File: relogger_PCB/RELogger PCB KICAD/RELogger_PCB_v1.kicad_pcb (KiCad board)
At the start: 2 copper layers, 115.6 x 99.1 mm, 76 parts, among them J1 RTC_MODULE, J2 Arduino_Nano_Header, J3 MICRO_SD, K1 ANEMOM1, P1 EXTERNAL PSU, P10 VANE, P11 SERIAL, P12 SOFT_SERIAL, P13 D6_D7, P14 AC_IN, P15 ANEMOM2, P2 BATTERY, P22 A_IN_45, P23 AGND_GND, P26 JMP_HALL, P3 SOLAR, P4 A_IN_01, P5 A_IN_23, P6 I2C_1, P7 I2C_2, P8 V_EXT, P9 3V3_VREF, Q2 RFU9110PBF, SW1 CALIBRATE, SW2 SW_PUSH_SMALL_H, SW3 ON/OFF, SW4 SW_PUSH_SMALL_H, U1 MCP3208, U2 MCP1826S, U3 LM2574, U5 MCP73832, U6 LM393

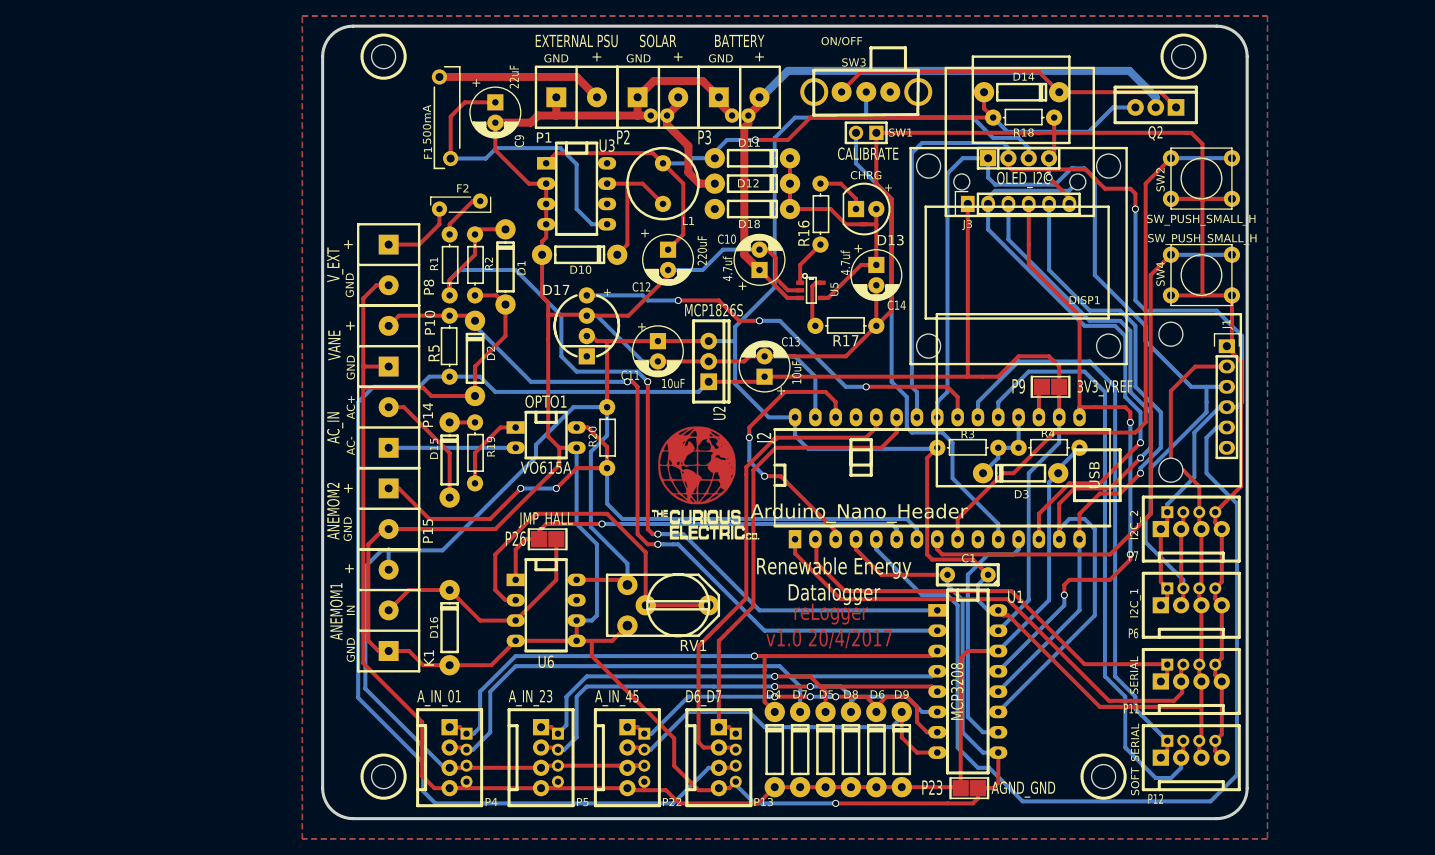
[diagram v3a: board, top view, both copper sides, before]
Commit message: Updated new scehmatic.
Still needs Freq conversion circuit. And 3.3V regulator
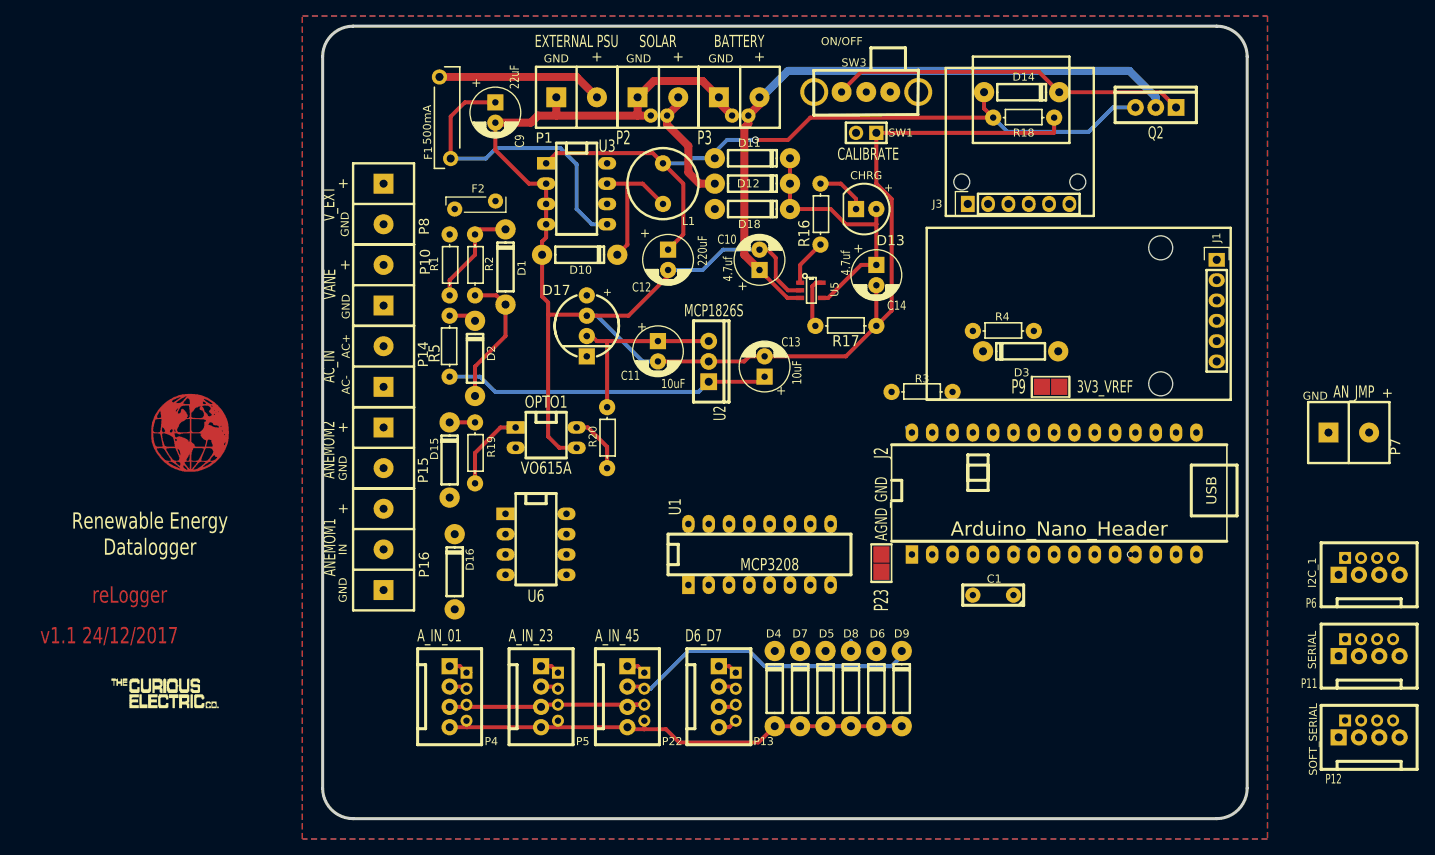
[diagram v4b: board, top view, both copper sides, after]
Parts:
- removed DISP1: OLED_I2C, REInnovationFootprint:TH_OLED1306
- removed HOLE1: CONN_1, 3mm_hole_relogger
- removed K1: ANEMOM1, REInnovationFootprint:SIL-3_screw_terminal
- removed P26: JMP_HALL, REInnovationFootprint:SM_2_SLDR_JMP
- removed RV1: 100k, REInnovationFootprint:RV_various_lg_pad
- removed SW2, SW4: SW_PUSH_SMALL_H, REInnovationFootprint:SW_PUSH_SMALL_lg_pad
- added P16: ANEMOM1, REInnovationFootprint:SIL-3_screw_terminal, F.Cu at (85.1, 103.5)
- D16: value 5V1 -> D
- P7: value I2C_2 -> AN_JMP; footprint matts_components:SIL-4_Grove_SIL -> REInnovationFootprint:SIL-2_screw_terminal
- moved LOGO2 70.8 mm to (50.8, 114.3)
- moved LOGO1 63.5 mm to (61.0, 83.8)
- moved U1 30.5 mm to (132.1, 99.1), turned to 0 degrees
- moved P23 28.3 mm to (147.3, 101.6), turned to 270 degrees
- moved P6 22.5 mm to (208.3, 101.6)
- moved P11 22.5 mm to (208.3, 111.8)
- moved P12 22.4 mm to (208.3, 121.9)
- moved P7 21.0 mm to (203.2, 83.8)
- moved R4 15.7 mm to (162.6, 71.1)
- moved D3 15.2 mm to (165.1, 73.7)
- moved J2 14.7 mm to (175.3, 91.4)
- moved J1 10.9 mm to (189.2, 62.2)
- moved R3 9.03 mm to (152.4, 78.7)
- moved U6 8.35 mm to (104.1, 101.6)
- moved P10 7.65 mm to (85.1, 67.9)
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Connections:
- D16 pad 1: /Hall_to_freq/Hall_In -> Net-(D16-Pad1)
- D16 pad 2: GND -> Net-(D16-Pad2)
- D17 pad 1: (no net) -> Net-(D17-Pad1)
- D18 pad 2: (no net) -> /Arduino Uno/5v
- J1 pad 6: (no net) -> Net-(J1-Pad6)
- J2 pad 10: (no net) -> /HC12_SET
- J2 pad 17: +3.3V -> /Power Supply/3V3_REF
- J2 pad 27: (no net) -> /Arduino Uno/5v
- J2 pad 30: /Vss -> /Arduino Uno/Vpower
- J2 pad 8: /SW_A -> /PWR_EXTI
- J2 pad 9: /SW_B -> /PWR_GPS
- LOGO1 pad 1: (no net) -> Net-(LOGO1-Pad1)
- P12 pad 4: GND -> Net-(P12-Pad4)
- P15 pad 1: /IN_ACFREQ -> /Hall_to_freq/Freq_IN
- P22 pad 1: /A4 -> Net-(P22-Pad1)
- P22 pad 3: /Vss -> Net-(P22-Pad3)
- P4 pad 1: /A0 -> Net-(P4-Pad1)
- P4 pad 3: /Vss -> Net-(P22-Pad3)
- P5 pad 1: /A2 -> Net-(P5-Pad1)
- P5 pad 3: /Vss -> Net-(P22-Pad3)
- P7 pad 1: /SCLK -> /Hall_to_freq/Freq_OUT2
- P7 pad 2: /SDA -> /IN_ACFREQ
- P9 pad 1: +3.3V -> /Power Supply/3V3_REF
- U6 pad 3: /Hall_to_freq/Hall_In -> Net-(R14-Pad2)
- U6 pad 5: GND -> Net-(R15-Pad2)
- U6 pad 6: GND -> Net-(C4-Pad1)
- U6 pad 7: (no net) -> /Hall_to_freq/Freq_OUT2
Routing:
- net GND: track 583.2 -> 225.9 mm, vias 2 -> 0
- net /Vss: track 376.6 -> 23.8 mm
- net +3.3V: track 243.6 -> 43.2 mm
- net GNDA: track 225.9 -> 79.1 mm
- net /SCLK: track 134.0 -> 0.00 mm, vias 1 -> 0
- net /SDA: track 132.1 -> 0.00 mm
- net /CLK_INT: track 118.0 -> 0.00 mm
- net /VEXT: track 107.8 -> 13.0 mm, vias 2 -> 0
- net /DIN_ADC: track 93.5 -> 0.00 mm, vias 1 -> 0
- net /VANE: track 96.6 -> 4.07 mm, vias 2 -> 0
- net /DOUT_ADC: track 78.9 -> 0.00 mm, vias 1 -> 0
- net /CLK_ADC: track 78.1 -> 0.00 mm, vias 3 -> 0
- net /IN_ACFREQ: track 84.8 -> 7.48 mm, vias 2 -> 0
- net /A0: track 76.2 -> 0.00 mm, vias 1 -> 0
- net /Tx_SOFT: track 76.0 -> 0.00 mm
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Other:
- board text added: "v1.1 24/12/2017"
- board text removed: "v1.0 20/4/2017"
